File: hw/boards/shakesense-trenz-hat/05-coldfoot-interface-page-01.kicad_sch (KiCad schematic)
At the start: 1 part, among them J4 FPGA test UART/reset

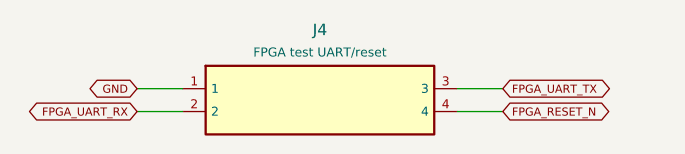
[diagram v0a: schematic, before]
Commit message: Expose Trenz GPIOs on the Pi-outline HDI sensor HAT
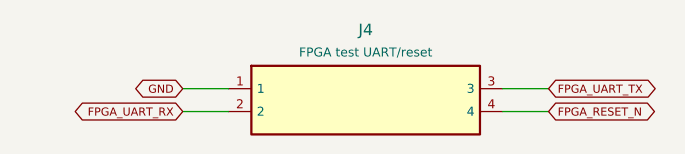
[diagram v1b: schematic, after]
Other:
- title: shakesense-trenz-hat / 05-coldfoot-interface-page-01 -> ShakeSense T1 / 05-coldfoot-interface-page-01
- moved on the sheet: J4
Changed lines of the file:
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@@
-(kicad_sch (version 20230121) (generator eeschema) (paper "A3") (title_block (title "shakesense-trenz-hat / 05-coldfoot-interface-page-01") (date "2026-09-23") (rev "A2 PROTOTYPE"))
-(symbol (lib_id "ShakeSense:Part_J4") (at 45.72 39.370000000000005 0) (unit 1) (in_bom yes) (on_board yes) (dnp no)
-              (property "Reference" "J4" (at 45.72 31.560000000000002 0) (effects (font (size 1.27 1.27))))
-              (property "Value" "FPGA test UART/reset" (at 45.72 34.06 0) (effects (font (size 1.0 1.0))))
-              (property "Footprint" "ShakeSense:Connector_PinHeader_2.54mm__PinHeader_1x04_P2.54mm_Vertical" (at 45.72 39.370000000000005 0) (effects (font (size 1 1)) hide))
-              (property "MPN" "Coldfoot UART service ONLY" (at 45.72 39.370000000000005 0) (effects (font (size 1 1)) hide))
+(kicad_sch (version 20230121) (generator eeschema) (paper "A3") (title_block (title "ShakeSense T1 / 05-coldfoot-interface-page-01") (date "2026-09-24") (rev "T1-GPIO"))
+(symbol (lib_id "ShakeSense:Part_J4") (at 50.8 39.370000000000005 0) (unit 1) (in_bom yes) (on_board yes) (dnp no)
+              (property "Reference" "J4" (at 50.8 31.560000000000002 0) (effects (font (size 1.27 1.27))))
+              (property "Value" "FPGA test UART/reset" (at 50.8 34.06 0) (effects (font (size 1.0 1.0))))
+              (property "Footprint" "ShakeSense:Connector_PinHeader_2.54mm__PinHeader_1x04_P2.54mm_Vertical" (at 50.8 39.370000000000005 0) (effects (font (size 1 1)) hide))
+              (property "MPN" "Coldfoot UART service ONLY" (at 50.8 39.370000000000005 0) (effects (font (size 1 1)) hide))
               (instances (project "shakesense-trenz-hat" (path "/4ffaaa5d-c728-540d-9f0f-f1cafbdbe36e/a8fb55ae-e6bc-58ff-ab76-d63aa5198255" (reference "J4") (unit 1)))))
-(wire (pts (xy 30.48 38.1) (xy 25.4 38.1)) (stroke (width 0) (type default)))
-(global_label "GND" (shape bidirectional) (at 25.4 38.1 180) (effects (font (size 0.9 0.9)) (justify right)))
-(wire (pts (xy 30.48 40.64) (xy 25.4 40.64)) (stroke (width 0) (type default)))
-(global_label "FPGA_UART_RX" (shape bidirectional) (at 25.4 40.64 180) (effects (font (size 0.9 0.9)) (justify right)))
-(wire (pts (xy 60.96 38.1) (xy 66.04 38.1)) (stroke (width 0) (type default)))
-(global_label "FPGA_UART_TX" (shape bidirectional) (at 66.04 38.1 0) (effects (font (size 0.9 0.9)) (justify left)))
-(wire (pts (xy 60.96 40.64) (xy 66.04 40.64)) (stroke (width 0) (type default)))
-(global_label "FPGA_RESET_N" (shape bidirectional) (at 66.04 40.64 0) (effects (font (size 0.9 0.9)) (justify left)))
+(wire (pts (xy 35.56 38.1) (xy 30.48 38.1)) (stroke (width 0) (type default)))
+(global_label "GND" (shape bidirectional) (at 30.48 38.1 180) (effects (font (size 0.9 0.9)) (justify right)))
+(wire (pts (xy 35.56 40.64) (xy 30.48 40.64)) (stroke (width 0) (type default)))
+(global_label "FPGA_UART_RX" (shape bidirectional) (at 30.48 40.64 180) (effects (font (size 0.9 0.9)) (justify right)))
+(wire (pts (xy 66.04 38.1) (xy 71.12 38.1)) (stroke (width 0) (type default)))
+(global_label "FPGA_UART_TX" (shape bidirectional) (at 71.12 38.1 0) (effects (font (size 0.9 0.9)) (justify left)))
+(wire (pts (xy 66.04 40.64) (xy 71.12 40.64)) (stroke (width 0) (type default)))
+(global_label "FPGA_RESET_N" (shape bidirectional) (at 71.12 40.64 0) (effects (font (size 0.9 0.9)) (justify left)))
 )
